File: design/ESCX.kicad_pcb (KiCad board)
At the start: 4 copper layers, 100 x 90 mm, 138 parts, among them J1 SWD, J10 Screw_Terminal_01x03, J11 Screw_Terminal_01x02, J2 Conn_Coaxial, J8 HALL_ENC, J9 USB_C_Receptacle_USB2.0_16P, Q1 IRF7854, Q2 IRF7854, Q3 IRF7854, Q4 IRF7854, Q5 IRF7854, Q6 IRF7854, SW1 SENSOR_VOLTAGE, U1 STM32F40X_LQFP64, U2 LM3671, U3 DRV8301, U4 nRF24L01P, U5 AD8418, U6 AD8418, U7 AD8418, X1 8MHz, X2 16MHz

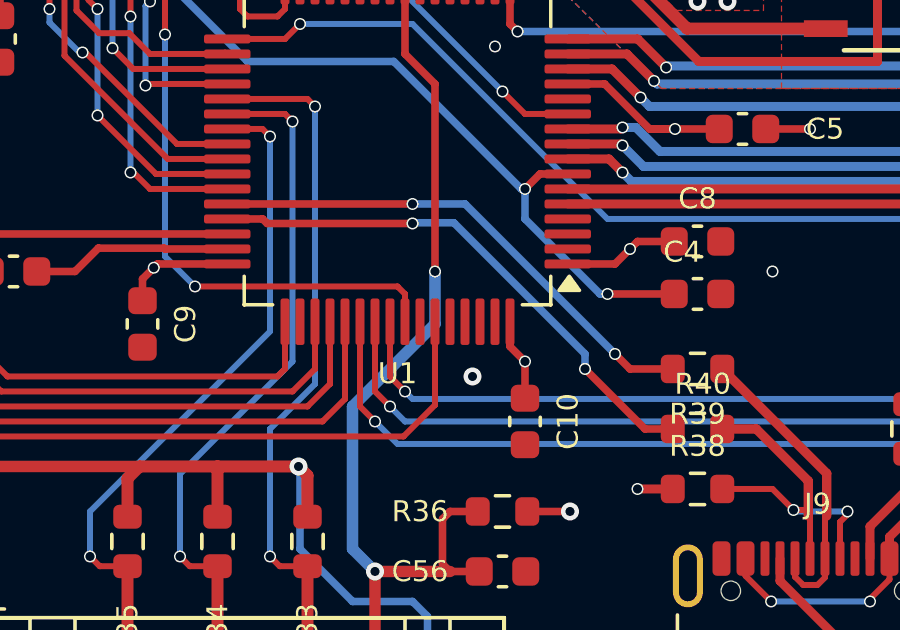
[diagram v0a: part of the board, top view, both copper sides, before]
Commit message: ruteo de USB
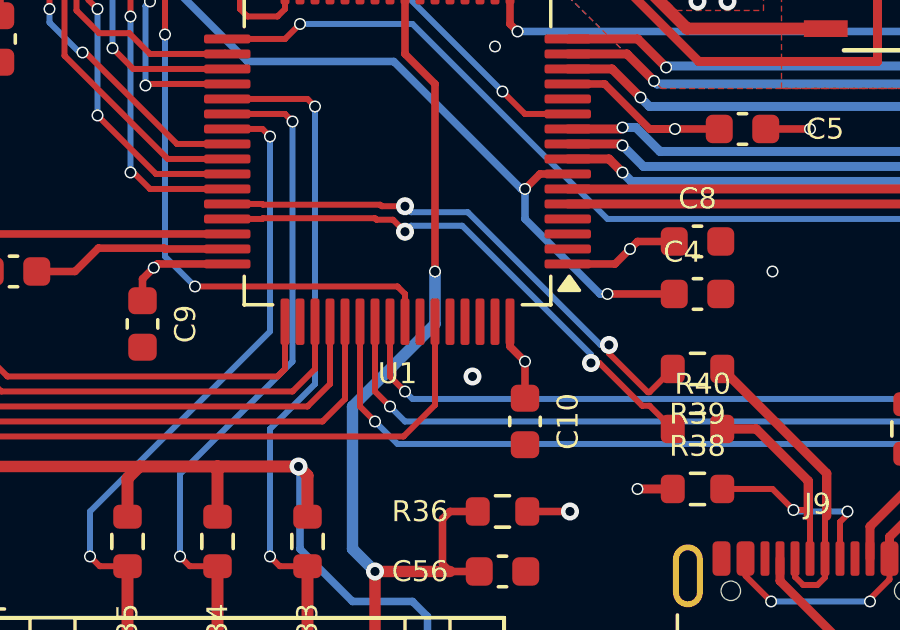
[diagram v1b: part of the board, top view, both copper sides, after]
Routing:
- net /MCU/USB_DN: track 17.1 -> 17.9 mm
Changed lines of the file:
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@@
+	)
+	(segment
+		(start 127.422206 112.775)
+		(end 127.472206 112.825)
+		(width 0.2)
+		(layer "F.Cu")
+		(net 79)
 	)
 	(segment
 		(start 137.175 118.25)
-		(end 135.75 118.25)
-		(width 0.254)
-		(layer "F.Cu")
-		(net 79)
-	)
-	(segment
-		(start 135.75 118.25)
-		(end 135.25 117.75)
-		(width 0.254)
+		(end 136.400001 119.024999)
+		(width 0.2)
+		(layer "F.Cu")
+		(net 79)
+	)
+	(segment
+		(start 136.343198 119.024999)
+		(end 135.050521 117.732322)
+		(width 0.2)
+		(layer "F.Cu")
+		(net 79)
+	)
+	(segment
+		(start 123.487501 112.75)
+		(end 123.512501 112.775)
+		(width 0.2)
+		(layer "F.Cu")
+		(net 79)
+	)
+	(segment
+		(start 123.512501 112.775)
+		(end 127.422206 112.775)
+		(width 0.2)
+		(layer "F.Cu")
+		(net 79)
+	)
+	(segment
+		(start 127.472206 112.825)
+		(end 128.25 112.825)
+		(width 0.2)
+		(layer "F.Cu")
+		(net 79)
+	)
+	(segment
+		(start 136.400001 119.024999)
+		(end 136.343198 119.024999)
+		(width 0.2)
 		(layer "F.Cu")
 		(net 79)
@@
 	(segment
 		(start 122.325 112.75)
-		(end 128.5 112.75)
-		(width 0.254)
-		(layer "F.Cu")
-		(net 79)
-	)
-	(via
-		(at 135.25 117.75)
-		(size 0.4)
-		(drill 0.3)
-		(layers "F.Cu" "B.Cu")
-		(net 79)
-	)
-	(via
-		(at 128.5 112.75)
-		(size 0.4)
-		(drill 0.3)
-		(layers "F.Cu" "B.Cu")
-		(net 79)
-	)
-	(segment
-		(start 128.5 112.75)
-		(end 130.25 112.75)
-		(width 0.254)
-		(layer "B.Cu")
-		(net 79)
-	)
-	(segment
-		(start 130.25 112.75)
-		(end 135.25 117.75)
-		(width 0.254)
+		(end 123.487501 112.75)
+		(width 0.2)
+		(layer "F.Cu")
+		(net 79)
+	)
+	(segment
+		(start 135.050521 117.732322)
+		(end 135.050521 117.449479)
+		(width 0.2)
+		(layer "F.Cu")
+		(net 79)
+	)
+	(via
+		(at 135.050521 117.449479)
+		(size 0.6)
+		(drill 0.3)
+		(layers "F.Cu" "B.Cu")
+		(net 79)
+	)
+	(via
+		(at 128.25 112.825)
+		(size 0.6)
+		(drill 0.3)
+		(layers "F.Cu" "B.Cu")
+		(net 79)
+	)
+	(segment
+		(start 128.449999 113.024999)
+		(end 128.25 112.825)
+		(width 0.2)
+		(layer "B.Cu")
+		(net 79)
+	)
+	(segment
+		(start 135.050521 117.449479)
+		(end 134.767678 117.449479)
+		(width 0.2)
+		(layer "B.Cu")
+		(net 79)
+	)
+	(segment
+		(start 130.343198 113.024999)
+		(end 128.449999 113.024999)
+		(width 0.2)
+		(layer "B.Cu")
+		(net 79)
+	)
+	(segment
+		(start 134.767678 117.449479)
+		(end 130.343198 113.024999)
+		(width 0.2)
 		(layer "B.Cu")
 		(net 79)
@@
 	(segment
 		(start 137.175 120.25)
-		(end 136.25 120.25)
-		(width 0.254)
-		(layer "F.Cu")
-		(net 80)
-	)
-	(segment
-		(start 136.25 120.25)
-		(end 134.25 118.25)
-		(width 0.254)
-		(layer "F.Cu")
-		(net 80)
-	)
-	(segment
-		(start 128.5 113.400002)
-		(end 123.654711 113.400002)
-		(width 0.254)
-		(layer "F.Cu")
-		(net 80)
-	)
-	(segment
-		(start 123.504709 113.25)
-		(end 122.325 113.25)
-		(width 0.254)
-		(layer "F.Cu")
-		(net 80)
-	)
-	(segment
-		(start 123.654711 113.400002)
-		(end 123.504709 113.25)
-		(width 0.254)
-		(layer "F.Cu")
-		(net 80)
-	)
-	(via
-		(at 134.25 118.25)
-		(size 0.4)
-		(drill 0.3)
-		(layers "F.Cu" "B.Cu")
-		(net 80)
-	)
-	(via
-		(at 128.5 113.400002)
-		(size 0.4)
-		(drill 0.3)
-		(layers "F.Cu" "B.Cu")
-		(net 80)
-	)
-	(segment
-		(start 128.523002 113.377)
-		(end 129.877 113.377)
-		(width 0.254)
-		(layer "B.Cu")
-		(net 80)
-	)
-	(segment
-		(start 128.5 113.400002)
-		(end 128.523002 113.377)
-		(width 0.254)
-		(layer "B.Cu")
-		(net 80)
-	)
-	(segment
-		(start 134.25 117.75)
-		(end 134.25 118.25)
-		(width 0.254)
-		(layer "B.Cu")
-		(net 80)
-	)
-	(segment
-		(start 129.877 113.377)
-		(end 134.25 117.75)
-		(width 0.254)
-		(layer "B.Cu")
-		(net 80)
+		(end 136.400001 119.475001)
+		(width 0.2)
+		(layer "F.Cu")
+		(net 80)
+	)
+	(segment
+		(start 134.732322 118.050521)
+		(end 134.449479 118.050521)
+		(width 0.2)
+		(layer "F.Cu")
+		(net 80)
+	)
+	(segment
+		(start 136.400001 119.475001)
+		(end 136.156802 119.475001)
+		(width 0.2)
+		(layer "F.Cu")
+		(net 80)
+	)
+	(segment
+		(start 123.487501 113.25)
+		(end 123.512501 113.225)
+		(width 0.2)
+		(layer "F.Cu")
+		(net 80)
+	)
+	(segment
+		(start 127.300001 113.275001)
+		(end 127.850001 113.275001)
+		(width 0.2)
+		(layer "F.Cu")
+		(net 80)
+	)
+	(segment
+		(start 122.325 113.25)
+		(end 123.487501 113.25)
+		(width 0.2)
+		(layer "F.Cu")
+		(net 80)
+	)
+	(segment
+		(start 136.156802 119.475001)
+		(end 134.732322 118.050521)
+		(width 0.2)
+		(layer "F.Cu")
+		(net 80)
+	)
+	(segment
+		(start 123.512501 113.225)
+		(end 127.25 113.225)
+		(width 0.2)
+		(layer "F.Cu")
+		(net 80)
+	)
+	(segment
+		(start 127.850001 113.275001)
+		(end 128.25 113.675)
+		(width 0.2)
+		(layer "F.Cu")
+		(net 80)
+	)
+	(segment
+		(start 127.25 113.225)
+		(end 127.300001 113.275001)
+		(width 0.2)
+		(layer "F.Cu")
+		(net 80)
+	)
+	(via
+		(at 128.25 113.675)
+		(size 0.6)
+		(drill 0.3)
+		(layers "F.Cu" "B.Cu")
+		(net 80)
+	)
+	(via
+		(at 134.449479 118.050521)
+		(size 0.6)
+		(drill 0.3)
+		(layers "F.Cu" "B.Cu")
+		(net 80)
+	)
+	(segment
+		(start 134.449479 118.050521)
+		(end 134.449479 117.767678)
+		(width 0.2)
+		(layer "B.Cu")
+		(net 80)
+	)
+	(segment
+		(start 134.449479 117.767678)
+		(end 130.156802 113.475001)
+		(width 0.2)
+		(layer "B.Cu")
+		(net 80)
+	)
+	(segment
+		(start 128.449999 113.475001)
+		(end 128.25 113.675)
+		(width 0.2)
+		(layer "B.Cu")
+		(net 80)
+	)
+	(segment
+		(start 130.156802 113.475001)
+		(end 128.449999 113.475001)
+		(width 0.2)
+		(layer "B.Cu")
+		(net 80)

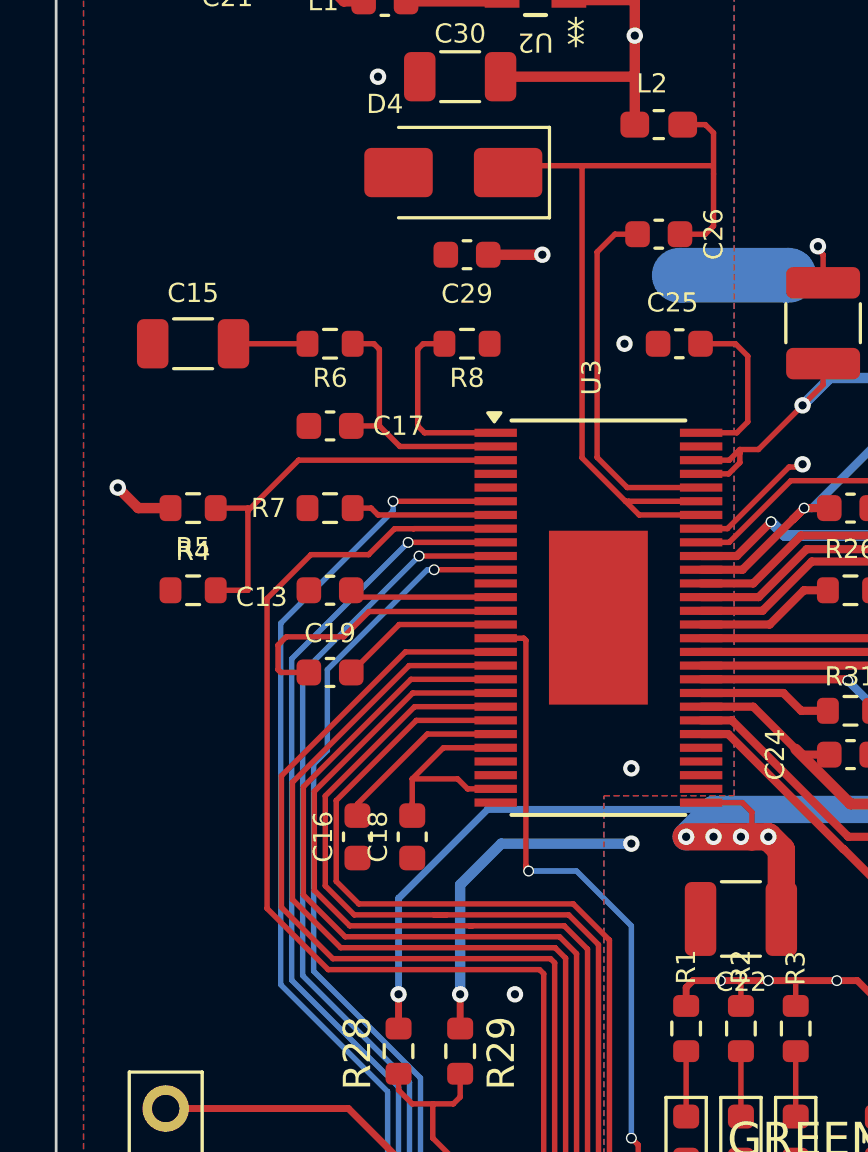
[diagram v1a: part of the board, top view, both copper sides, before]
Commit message: Cambios en posicion de capacitores de transistores
Tambien agregado de vias de tierra
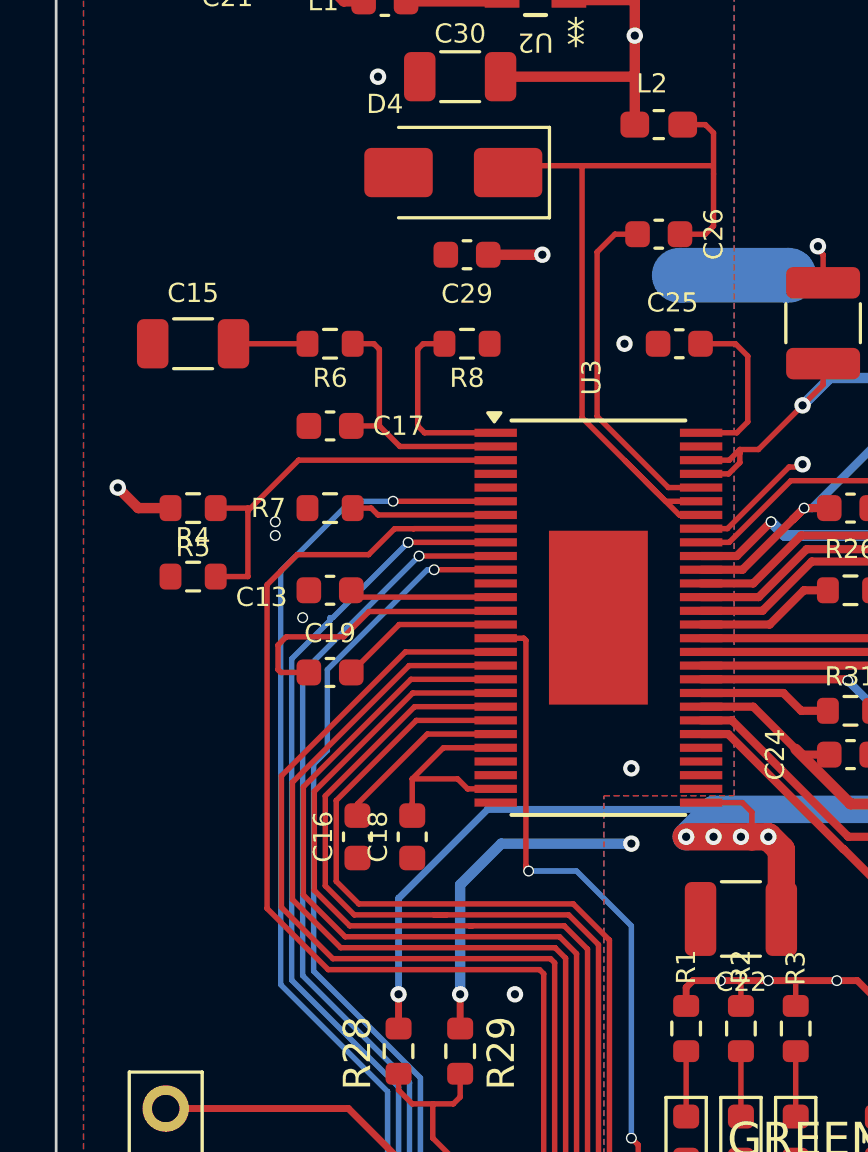
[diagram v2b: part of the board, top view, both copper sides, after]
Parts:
- moved R4 0.50 mm to (104.0, 79.5)
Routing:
- net /DRV8301/FAULT: track 71.2 -> 72.1 mm
- net Net-(U3-BST_BK): track 13.5 -> 12.6 mm
- net Net-(U3-VSENSE): track 15.2 -> 14.7 mm
- net GND1: vias 26 -> 29

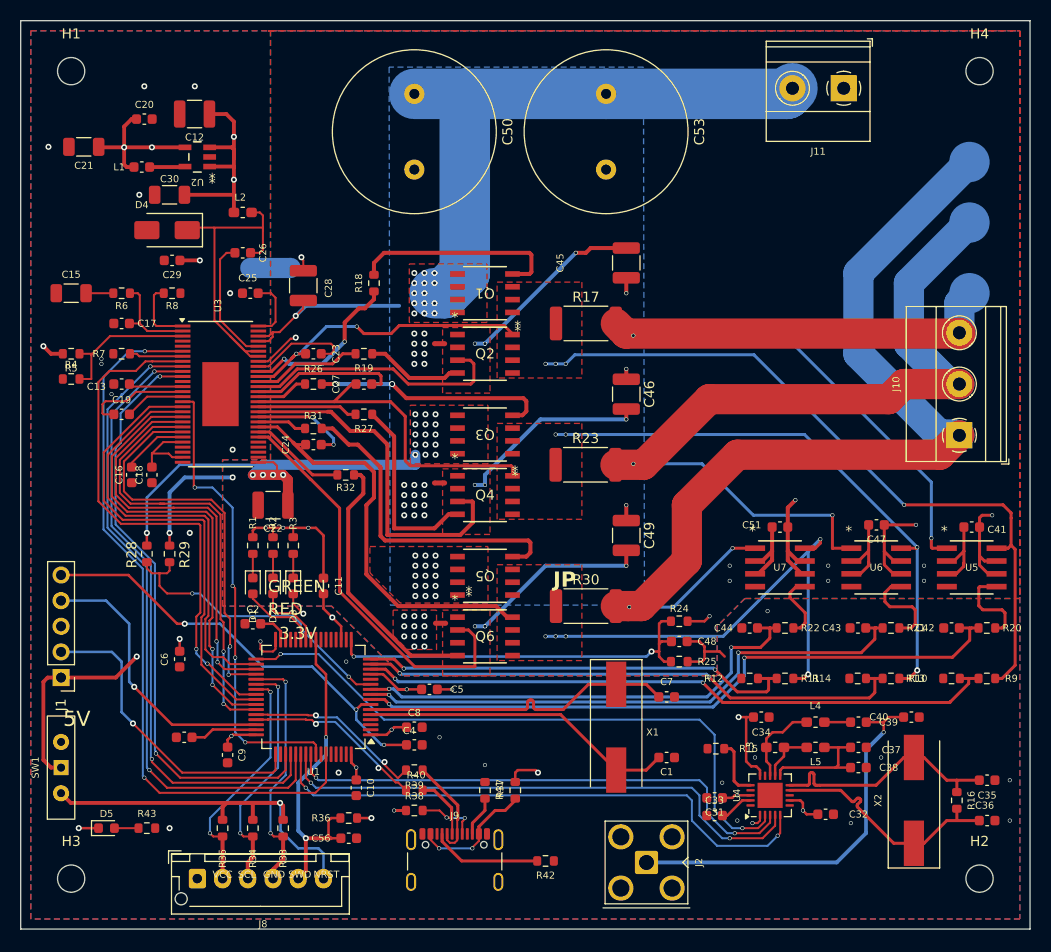
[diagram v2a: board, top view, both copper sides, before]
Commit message: Cambios a constraints
Cambios de constraints de ancho mínimo para pasar DRC
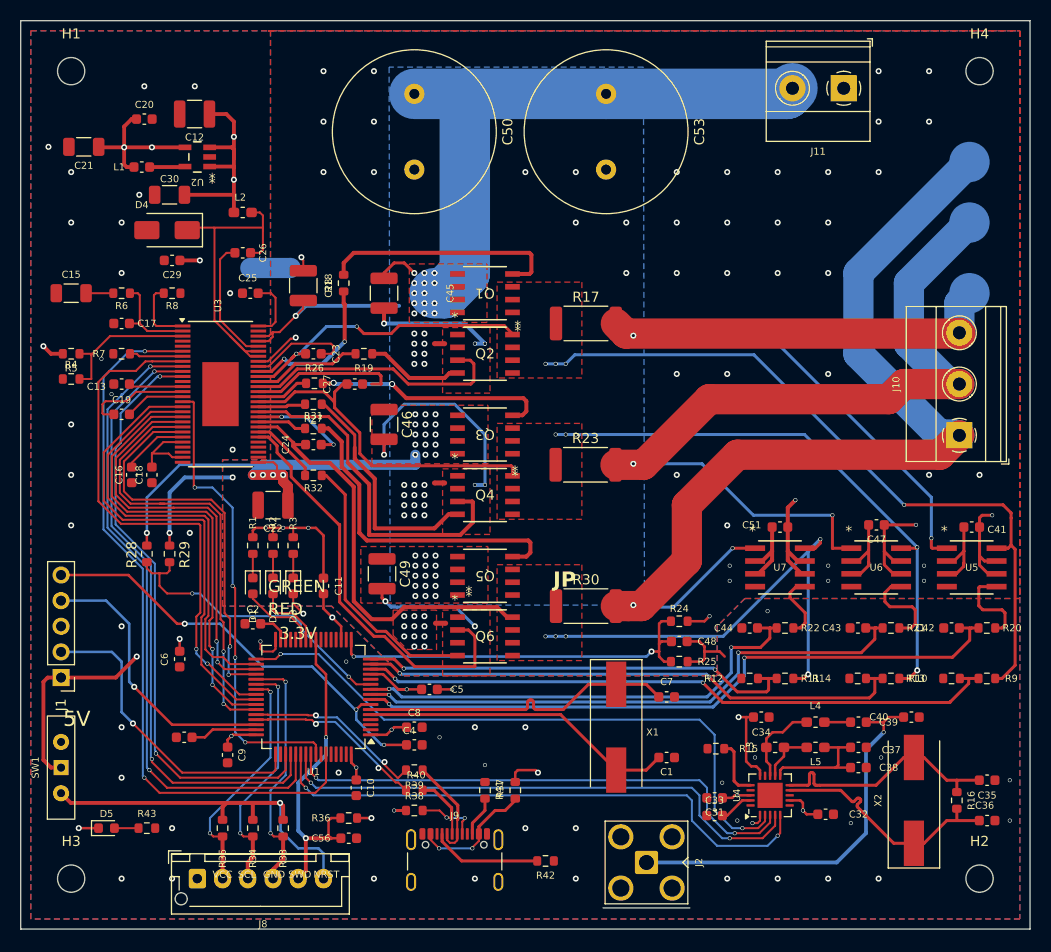
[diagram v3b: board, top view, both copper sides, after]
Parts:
- moved C49 24.5 mm to (134.8, 98.8)
- moved C45 24.2 mm to (135.0, 71.0), turned to -90 degrees
- moved C46 24.2 mm to (135.0, 84.0)
- moved R27 5.10 mm to (128.0, 82.0)
- moved R32 3.20 mm to (128.0, 89.0)
- moved R18 3.00 mm to (131.0, 70.0)
- moved C27 0.90 mm to (132.1, 80.0)
- moved R26 0.12 mm to (128.1, 79.9)
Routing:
- net /DRV8301/SL_C: track 59.7 -> 52.7 mm, vias 3 -> 2
- net /DRV8301/SL_A: track 45.2 -> 39.7 mm
- net /DRV8301/GL_B: track 9.94 -> 4.73 mm
- net Net-(Q4-Pad1): track 19.1 -> 23.4 mm
- net /power/G1: track 20.9 -> 23.9 mm
- net /DRV8301/GL_C: track 9.51 -> 6.88 mm
- net /DRV8301/SL_B: track 54.9 -> 57.5 mm
- net /DRV8301/GH_A: track 16.7 -> 15.2 mm
- net /power/PH_A: track 84.8 -> 83.9 mm
- net /DRV8301/SH_C: track 90.2 -> 91.0 mm
- net SUPPLY: track 126.6 -> 126.9 mm, vias 53 -> 50
- net GND2: vias 39 -> 74
- net GND1: vias 29 -> 51

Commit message: Cambios en numero de partes
Updeteados algunos numeros de JLCPCB
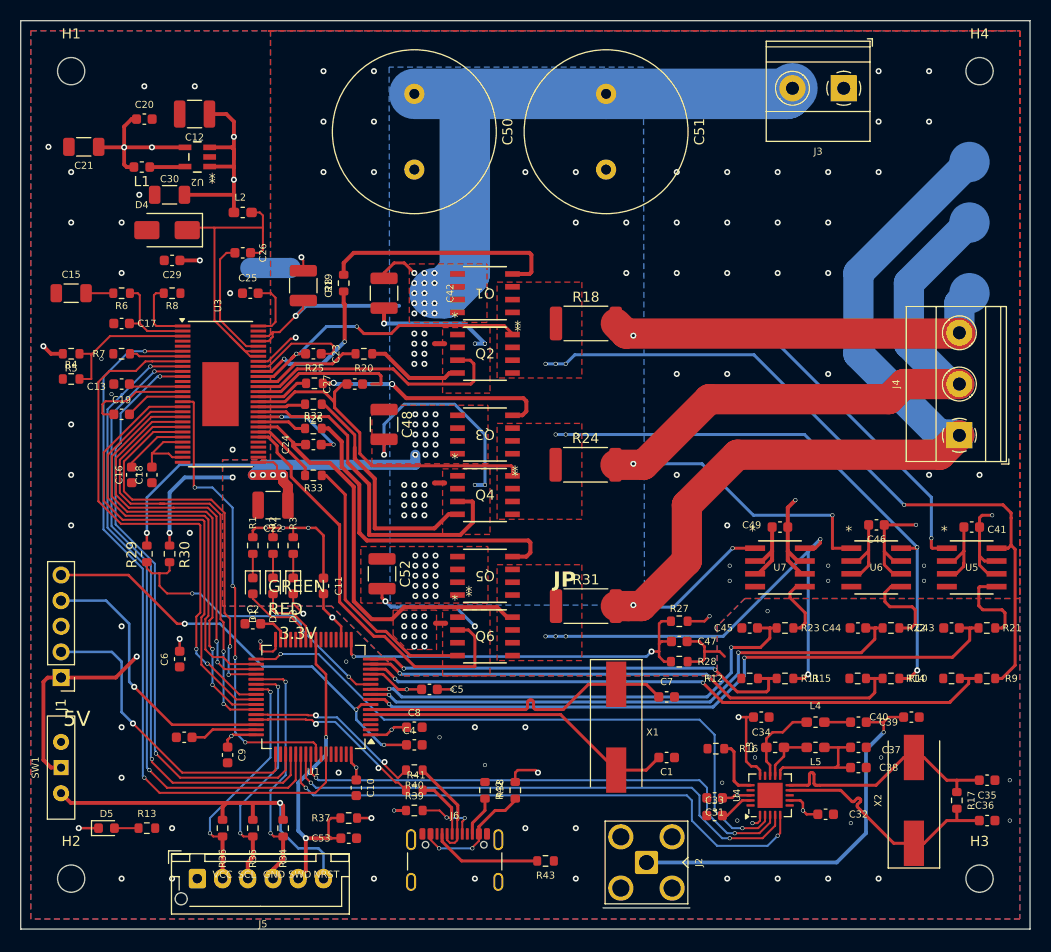
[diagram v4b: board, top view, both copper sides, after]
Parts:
- D1, D5: value LED_Filled -> Red LED
- D2: value LED_Filled -> Green LED
- D3: value LED_Filled -> Blue LED
- D4: value DIODE -> Schottky Diodes
- L1: value 2.2uF -> 2.2uH; footprint Capacitor_SMD:C_0603_1608Metric -> Inductor_SMD:L_0603_1608Metric
- renumbered C45 to C42, C42 to C43, C43 to C44, C44 to C45, C47 to C46, C48 to C47, C46 to C48, C51 to C49, C53 to C51, C49 to C52, C56 to C53, H3 to H2, H2 to H3, J11 to J3, J10 to J4, J8 to J5, J9 to J6, R43 to R13, R13 to R14, R14 to R15, R15 to R16, R16 to R17, R17 to R18, R18 to R19, R19 to R20, R20 to R21, R21 to R22, R22 to R23, R23 to R24, R26 to R25, R27 to R26, R24 to R27, R25 to R28, R28 to R29, R29 to R30, R30 to R31, R31 to R32, R32 to R33, R33 to R34, R34 to R35, R35 to R36, R36 to R37, R37 to R38, R38 to R39, R39 to R40, R40 to R41, R41 to R42, R42 to R43
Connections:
- SW1 pad 1: +3.3V -> +5V
- SW1 pad 3: +5V -> +3.3V

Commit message: Correccion de algunos DRC
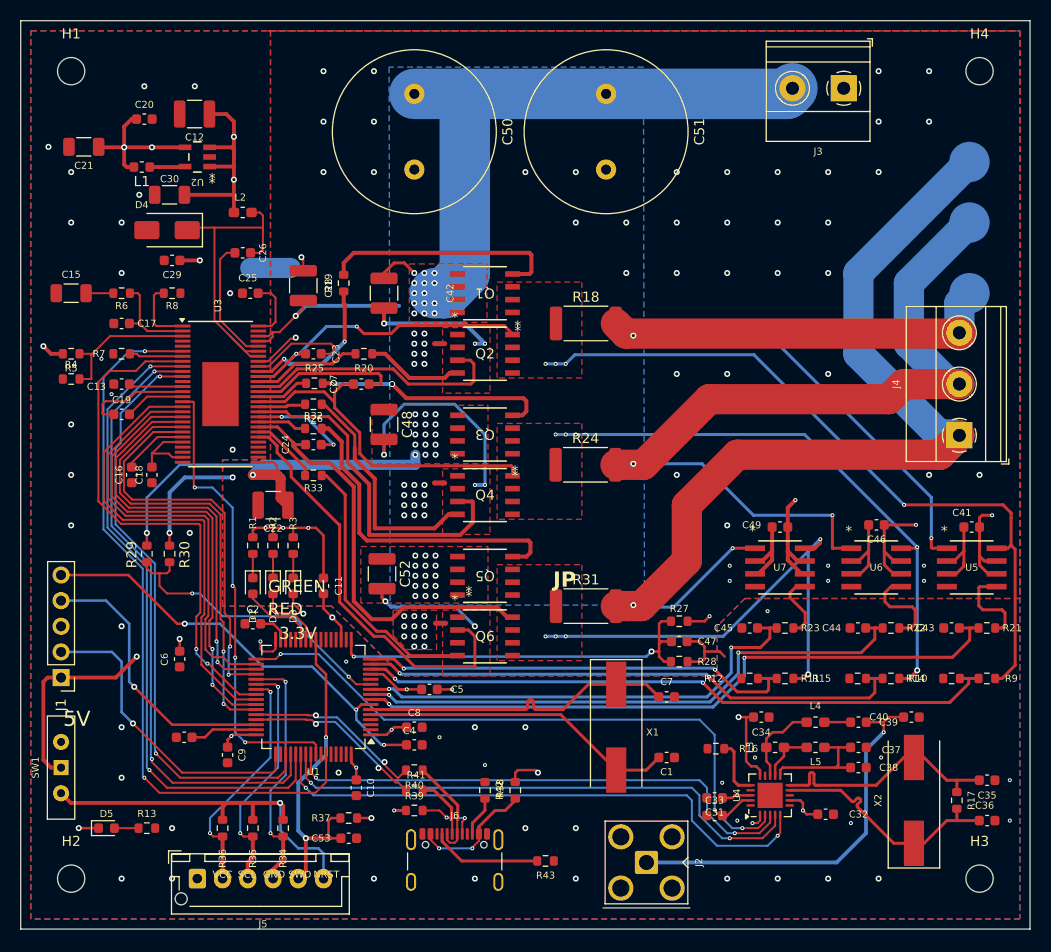
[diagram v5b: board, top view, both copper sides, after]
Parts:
- moved C27 0.65 mm to (132.8, 80.0)
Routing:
- net SUPPLY: track 126.9 -> 126.6 mm, vias 50 -> 47
